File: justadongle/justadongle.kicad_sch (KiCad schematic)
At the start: 12 parts, among them U1 SL2.1A_C6798314

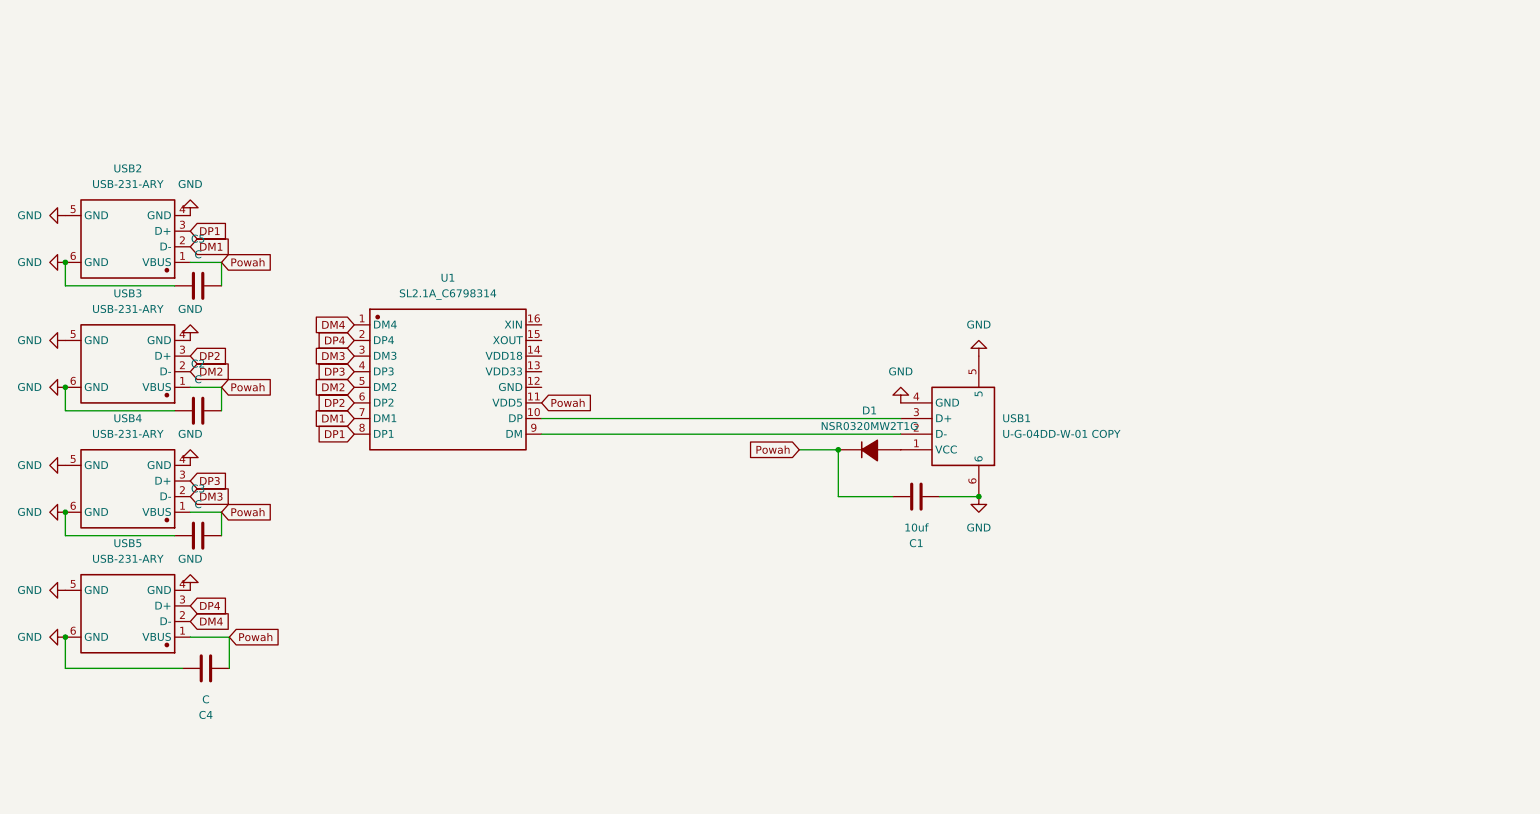
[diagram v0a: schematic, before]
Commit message: Figured out all the stuff except for the sel logic and havent started on the female ports other than USB-A yet
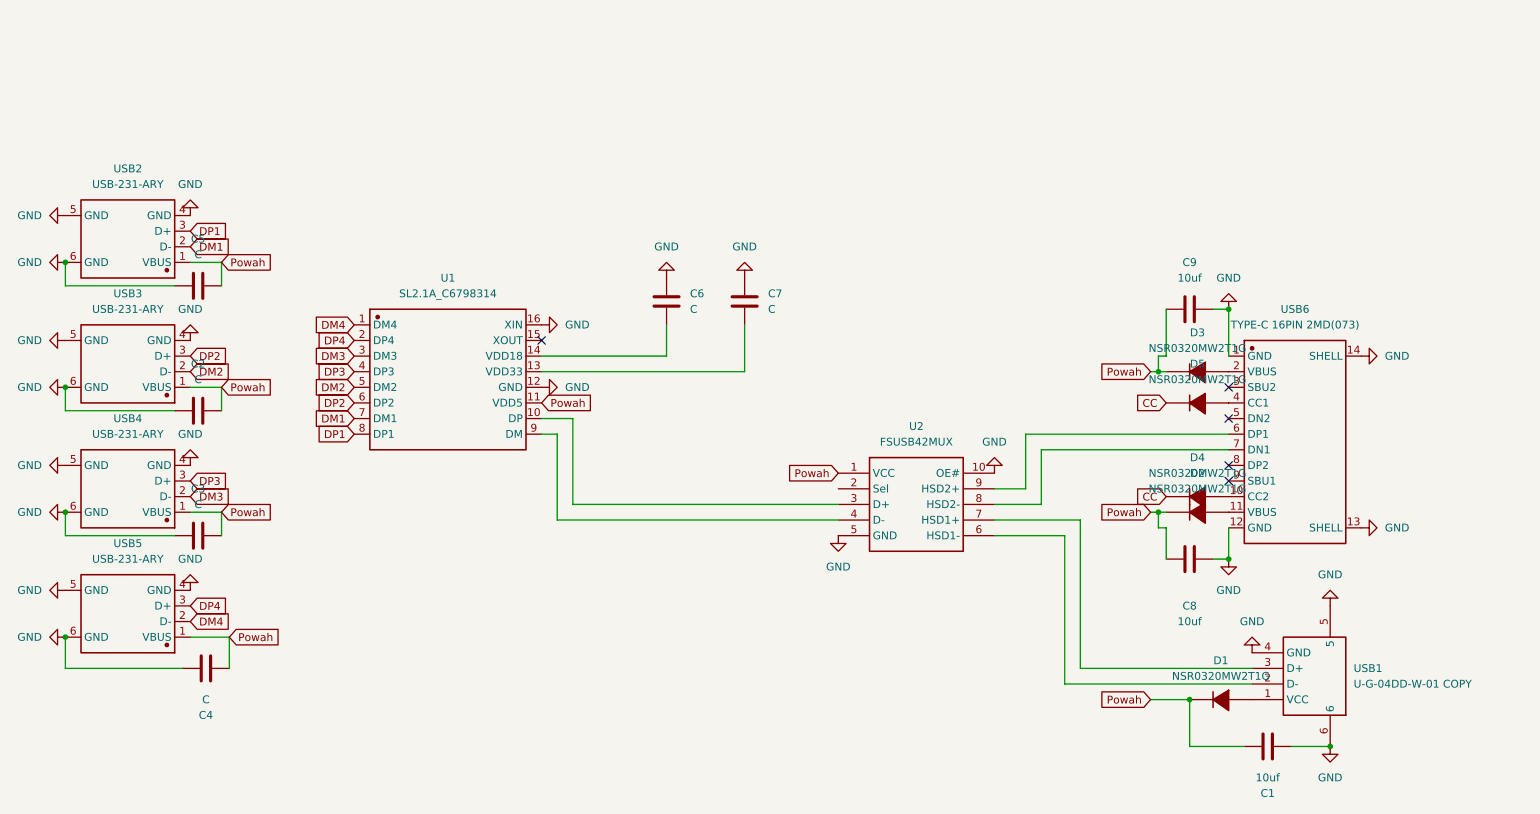
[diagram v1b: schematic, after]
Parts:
- added C6, C7: C, symbol Device:C
- added C8, C9: 10uf, symbol Device:C
- added D2, D3, D4, D5: NSR0320MW2T1G, symbol SCHLIB_NSR0320MW2T1G_2025-08-14:NSR0320MW2T1G
- added U2: FSUSB42MUX, symbol SCHLIB_FSUSB42MUX_2025-08-14:FSUSB42MUX
- added USB6: TYPE-C 16PIN 2MD(073), symbol SCHLIB_TYPE-C-16PIN-2MD(073)_2025-08-14 (1):TYPE-C 16PIN 2MD(073)
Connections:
- net GND: now also U1.12 (GND), U1.16 (XIN), C6.1, C7.1, C8.1, C9.1, U2.10 (OE#), U2.5 (GND), USB6.1 (GND), USB6.12 (GND), USB6.13 (SHELL), USB6.14 (SHELL)
- net Powah: now also C8.2, C9.2, D2.1 (C), D3.1 (C), U2.1 (VCC)
- net at U1.10 (DP): now also U2.3 (D+); no longer USB1.3 (D+)
- net at U1.13 (VDD33): now also C7.2
- net at U1.14 (VDD18): now also C6.2
- net at U1.9 (DM): now also U2.4 (D-); no longer USB1.2 (D-)
- new net: D4.2 (A), USB6.10 (CC2)
- new net: D5.2 (A), USB6.4 (CC1)
- new net: D2.2 (A), USB6.11 (VBUS)
- new net: D3.2 (A), USB6.2 (VBUS)
- new net: U2.9 (HSD2+), USB6.6 (DP1)
- new net: U2.8 (HSD2-), USB6.7 (DN1)
- new net: U2.6 (HSD1-), USB1.2 (D-)
- new net: U2.7 (HSD1+), USB1.3 (D+)
- new net CC: D4.1 (C), D5.1 (C)
- no-connect marks 0 -> 5
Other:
- moved on the sheet: C1, D1, USB1

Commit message: Completed the USB-A and USB-C interchangeable and automatic switcheroo thingy to detetct which connector is plugged in and automatically switch to it
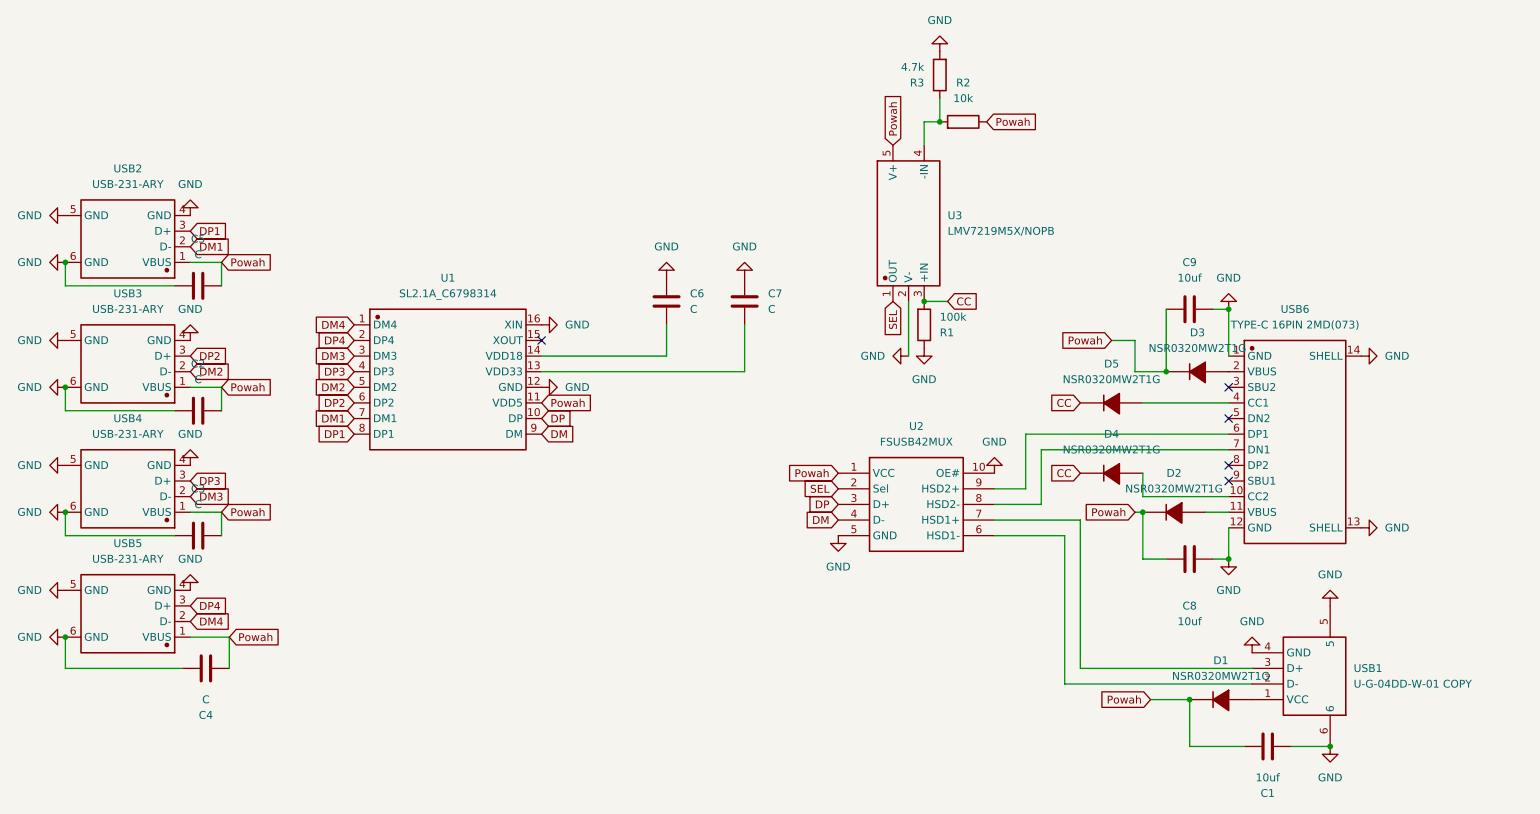
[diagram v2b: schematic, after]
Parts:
- added R1: 100k, symbol Device:R
- added R2: 10k, symbol Device:R
- added R3: 4.7k, symbol Device:R
- added U3: LMV7219M5X/NOPB, symbol SCHLIB_LMV7219M5X-NOPB_2025-08-14:LMV7219M5X/NOPB
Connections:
- net CC: now also R1.2, U3.3 (+IN)
- net GND: now also R1.1, R3.2, U3.2 (V-)
- net Powah: now also R2.1, U3.5 (V+)
- net DP: now reaches U1.10 (DP), U2.3 (D+)
- net DM : now reaches U1.9 (DM), U2.4 (D-)
- net SEL: now reaches U2.2 (Sel)
- net SEL: now also U3.1 (OUT)
- new net: R2.2, R3.1, U3.4 (-IN)
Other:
- moved on the sheet: D2, D4, D5

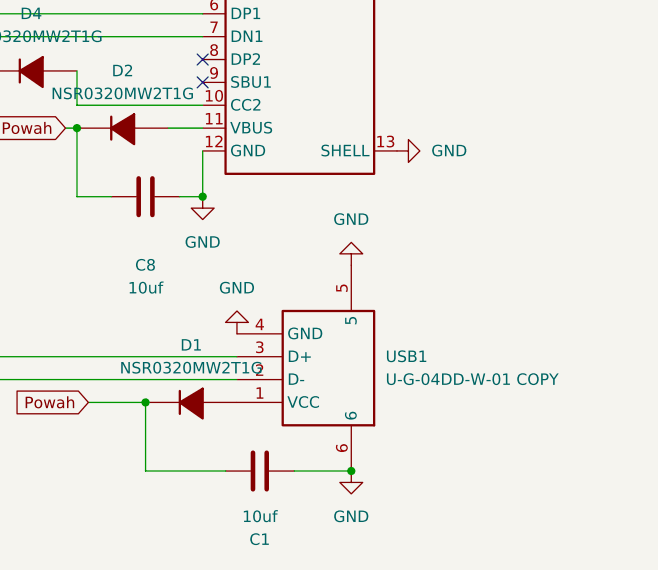
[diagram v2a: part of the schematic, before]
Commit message: replaced the USB 2.0 Connector with USB 3.0 for extra power
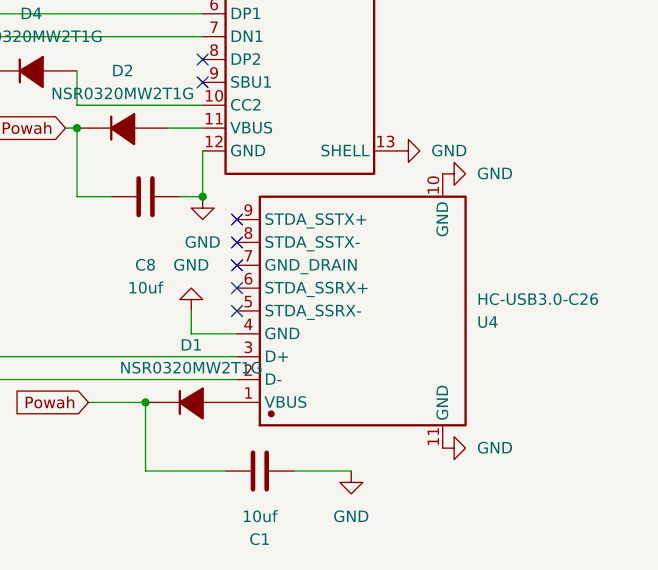
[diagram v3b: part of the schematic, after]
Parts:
- removed USB1: U-G-04DD-W-01 COPY, symbol SCHLIB_U-G-04DD-W-01-COPY_2025-08-14:U-G-04DD-W-01 COPY
- added U4: HC-USB3.0-C26, symbol SCHLIB_HC-USB3.0-C26_2025-08-14:HC-USB3.0-C26
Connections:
- net GND: now also U4.10 (GND), U4.11 (GND), U4.4 (GND)
- net at D1.2 (A): now also U4.1 (VBUS)
- net at U2.6 (HSD1-): now also U4.2 (D-)
- net at U2.7 (HSD1+): now also U4.3 (D+)
- no-connect marks 5 -> 10
